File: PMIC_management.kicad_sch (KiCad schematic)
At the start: 24 parts, among them SW1 SW_Push, SW2 SW_Push, U3 RK809, Y1 32.768Khz

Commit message: PMIC DCDC
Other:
- company: (none) -> Qingdao IotPi Information Technology
- title: (none) -> Leaf RV1126 PMIC RK809
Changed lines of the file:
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@@
 (kicad_sch (version 20230121) (generator eeschema)
   (paper "A4")
+  (title_block
+    (title "Leaf RV1126 PMIC RK809")
+    (date "2023-02-23")
+    (rev "1")
+    (company "Qingdao IotPi Information Technology")
+  )
   (junction (at 86.36 67.31) (diameter 0) (color 0 0 0 0)
   )

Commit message: updated PMIC DCDC
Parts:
- added TP1: TestPoint, symbol Connector:TestPoint
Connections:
- net at U3.60 (EXT_EN): now also TP1.1
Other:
- note added: "还需要考虑充电/保护电路"
- note added: "需要与 RK809 的 DataSheet中的参 考电路(双电池)的 设计对比"
- moved on the sheet: C8, D3, SW2

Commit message: updated: PMIC codec
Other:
- title: Leaf RV1126 PMIC RK809 -> Leaf RV1126 PMIC RK809 Codec
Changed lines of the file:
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@@
   (paper "A4")
   (title_block
-    (title "Leaf RV1126 PMIC RK809")
-    (date "2023-02-23")
+    (title "Leaf RV1126 PMIC RK809 Codec")
+    (date "2023-02-25")
     (rev "1")
     (company "Qingdao IotPi Information Technology")

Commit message: updated: PMIC
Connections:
- net PMIC_CLK_32K renamed CLK_32K
- net PMIC_I2C_SCL renamed I2C_SCL
- net PMIC_I2C_SDA renamed I2C_SDA
- net PMIC_INT renamed INT
- net PMIC_RESET renamed RESET
- net PMIC_SLEEP renamed SLEEP
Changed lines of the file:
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@@
     )
   )
-  (hierarchical_label "PMIC_I2C_SCL" (shape input) (at 38.1 24.13 180) (fields_autoplaced)
+  (hierarchical_label "I2C_SCL" (shape input) (at 38.1 24.13 180) (fields_autoplaced)
     (effects (font (size 1.27 1.27)) (justify right))
   )
-  (hierarchical_label "PMIC_INT" (shape output) (at 38.1 31.75 180) (fields_autoplaced)
+  (hierarchical_label "INT" (shape output) (at 38.1 31.75 180) (fields_autoplaced)
     (effects (font (size 1.27 1.27)) (justify right))
   )
-  (hierarchical_label "PMIC_CLK_32K" (shape output) (at 38.1 29.21 180) (fields_autoplaced)
+  (hierarchical_label "CLK_32K" (shape output) (at 38.1 29.21 180) (fields_autoplaced)
     (effects (font (size 1.27 1.27)) (justify right))
   )
-  (hierarchical_label "PMIC_I2C_SDA" (shape bidirectional) (at 38.1 26.67 180) (fields_autoplaced)
+  (hierarchical_label "I2C_SDA" (shape bidirectional) (at 38.1 26.67 180) (fields_autoplaced)
     (effects (font (size 1.27 1.27)) (justify right))
   )
-  (hierarchical_label "PMIC_RESET" (shape bidirectional) (at 38.1 36.83 180) (fields_autoplaced)
+  (hierarchical_label "RESET" (shape bidirectional) (at 38.1 36.83 180) (fields_autoplaced)
     (effects (font (size 1.27 1.27)) (justify right))
   )
-  (hierarchical_label "PMIC_SLEEP" (shape input) (at 38.1 34.29 180) (fields_autoplaced)
+  (hierarchical_label "SLEEP" (shape input) (at 38.1 34.29 180) (fields_autoplaced)
     (effects (font (size 1.27 1.27)) (justify right))
   )

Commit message: updated: titles
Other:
- title: Leaf RV1126 PMIC RK809 Codec -> Leaf RV1126 RK809 Management
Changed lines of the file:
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@@
   (paper "A4")
   (title_block
-    (title "Leaf RV1126 PMIC RK809 Codec")
+    (title "Leaf RV1126 RK809 Management")
     (date "2023-02-25")
     (rev "1")

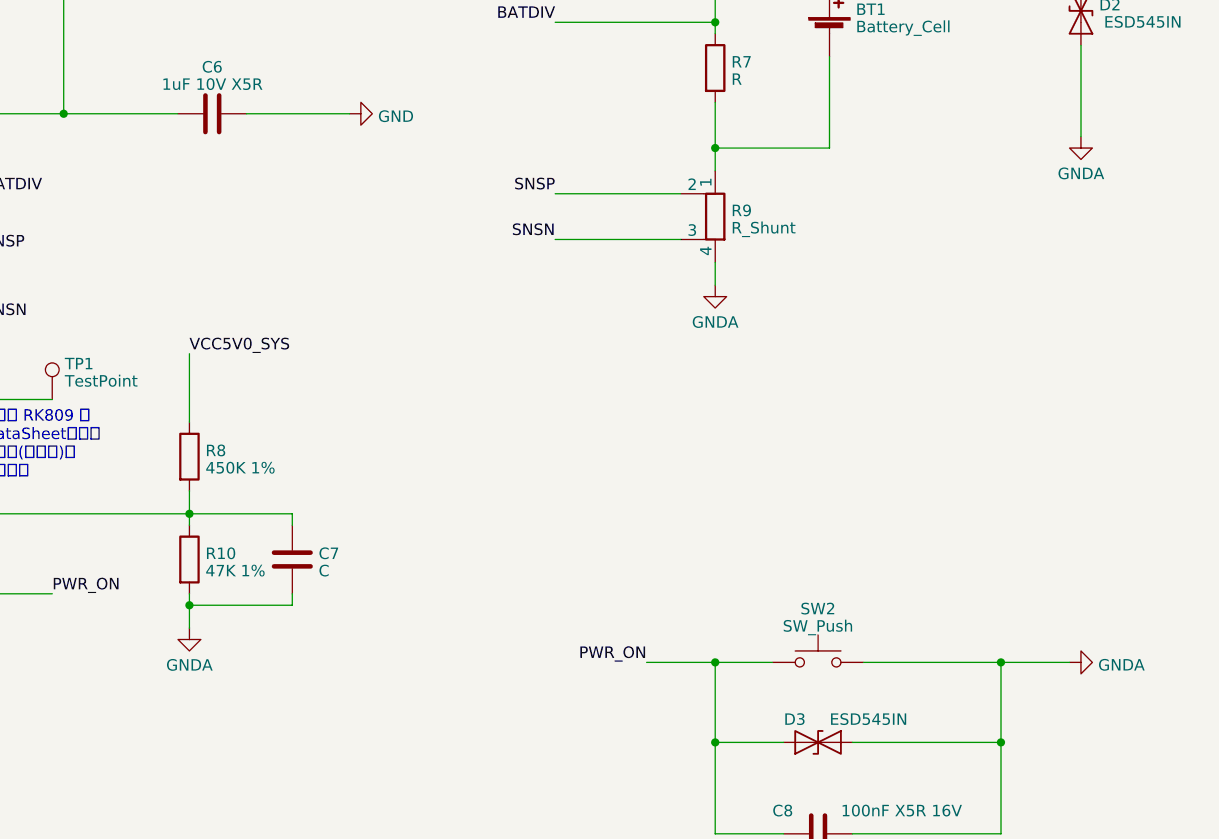
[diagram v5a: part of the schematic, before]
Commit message: changed to use GND instead of GNDD and GNDA
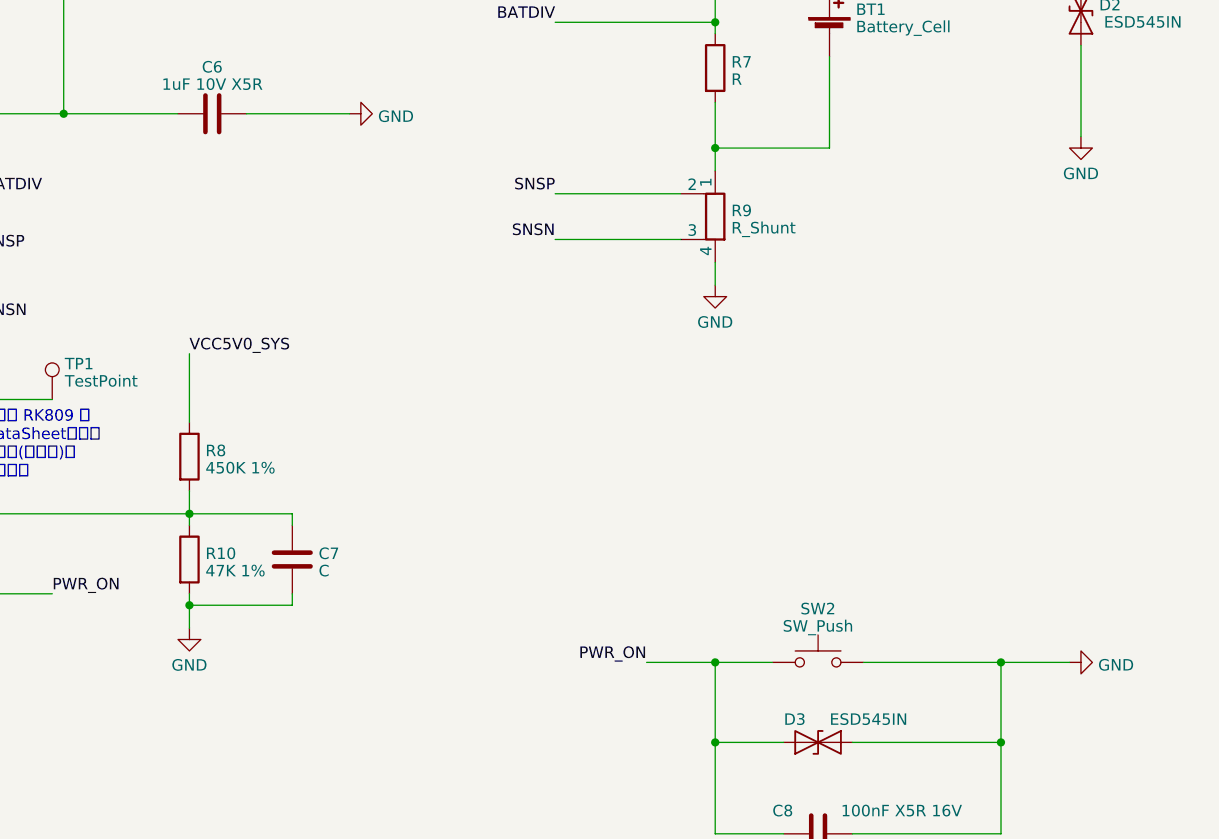
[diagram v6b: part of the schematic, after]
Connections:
- net GNDA is gone; now on net GND: C7.2, C8.2, D2.1 (A1), D3.1 (A1), R10.2, R9.4, SW2.2

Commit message: Updated eMMC
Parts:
- U3: value RK809 -> RK809-2
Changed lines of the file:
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@@
       (effects (font (size 1.27 1.27)))
     )
-    (property "Value" "RK809" (at 120.65 76.2 0)
+    (property "Value" "RK809-2" (at 120.65 76.2 0)
       (effects (font (size 1.27 1.27)))
     )

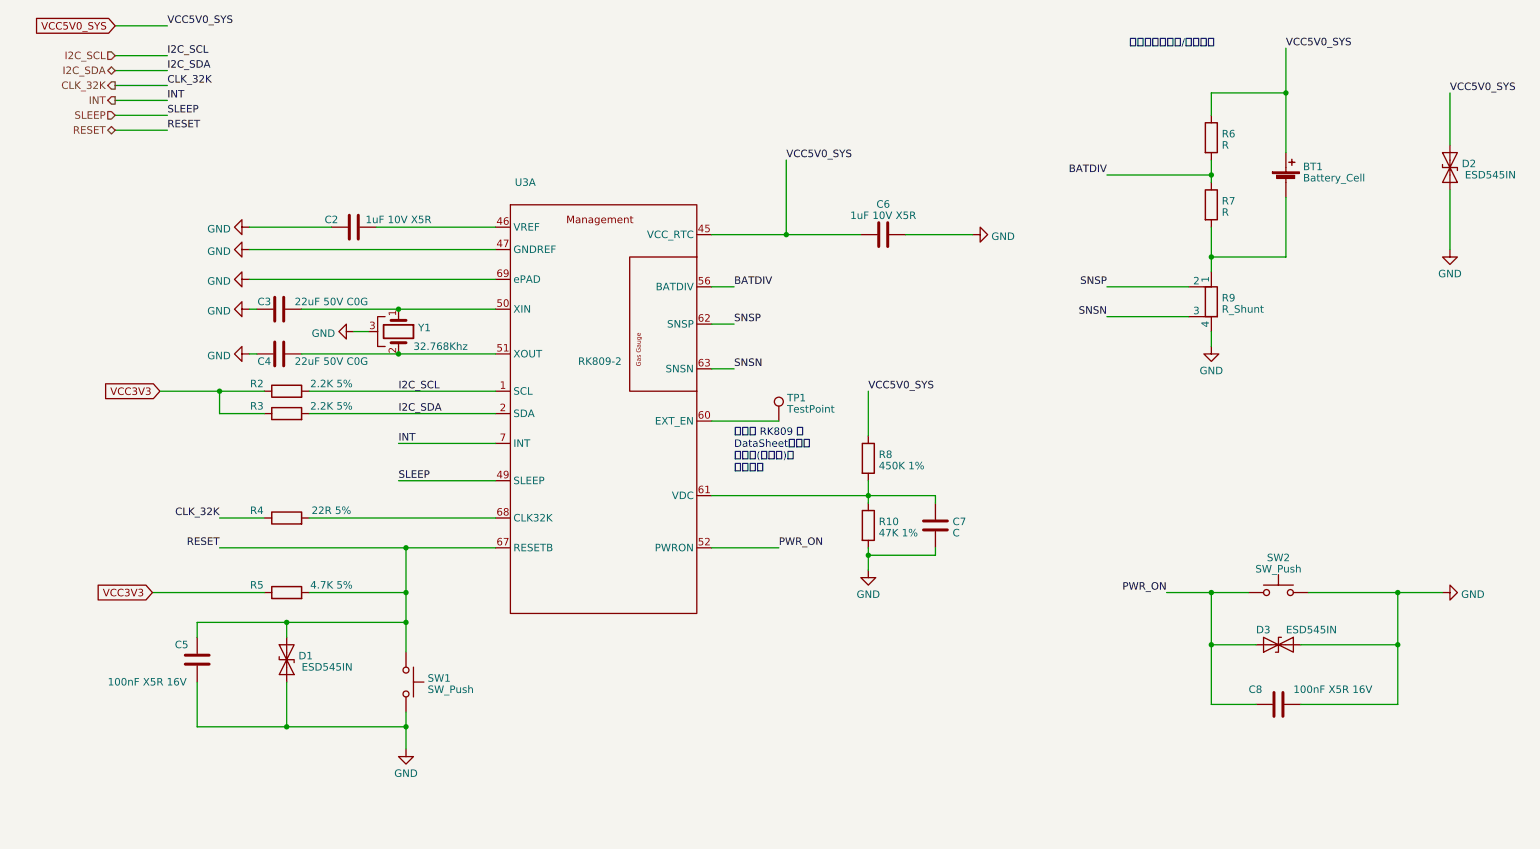
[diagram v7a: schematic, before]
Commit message: updated footprints
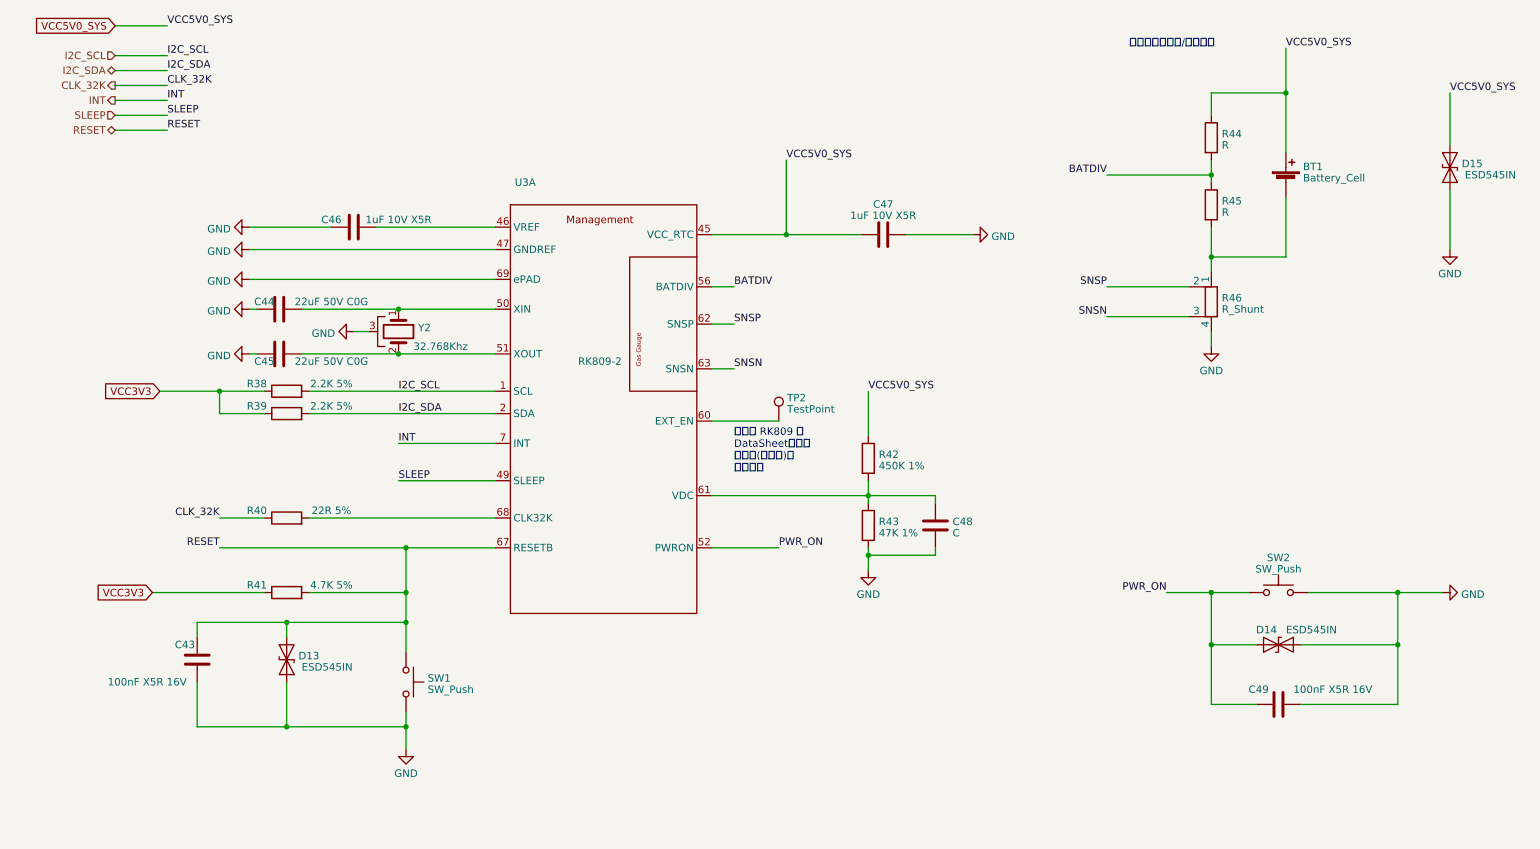
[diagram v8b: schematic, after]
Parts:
- renumbered C5 to C43, C3 to C44, C4 to C45, C2 to C46, C6 to C47, C7 to C48, C8 to C49, D1 to D13, D3 to D14, D2 to D15, R2 to R38, R3 to R39, R4 to R40, R5 to R41, R8 to R42, R10 to R43, R6 to R44, R7 to R45, R9 to R46, TP1 to TP2, Y1 to Y2
